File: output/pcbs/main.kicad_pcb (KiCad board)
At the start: 2 copper layers, 125.8 x 86.6 mm, 22 parts

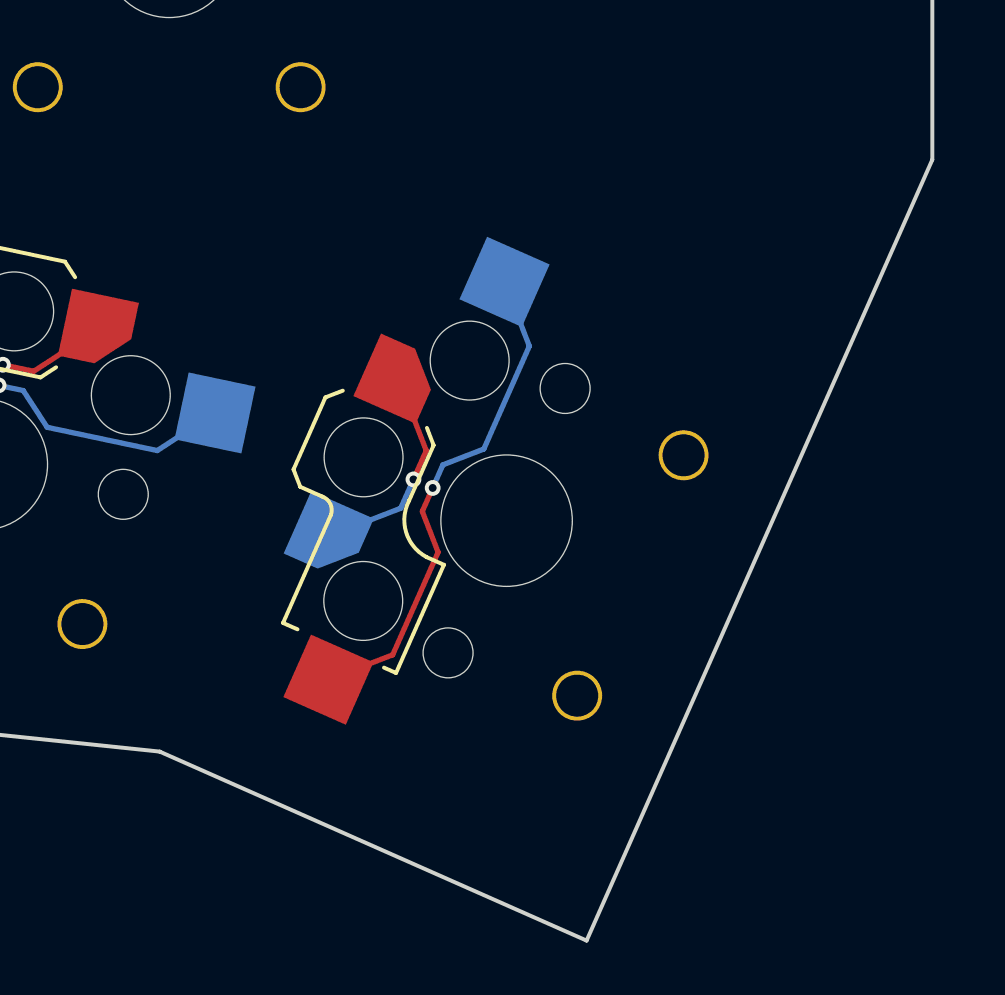
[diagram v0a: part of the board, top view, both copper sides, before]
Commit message: feat: add bottom ring bottom right corner ref
feat: add (bottom inner br, mcu tl) - (inner thumb tr, inner thumb tl)
lines intersection
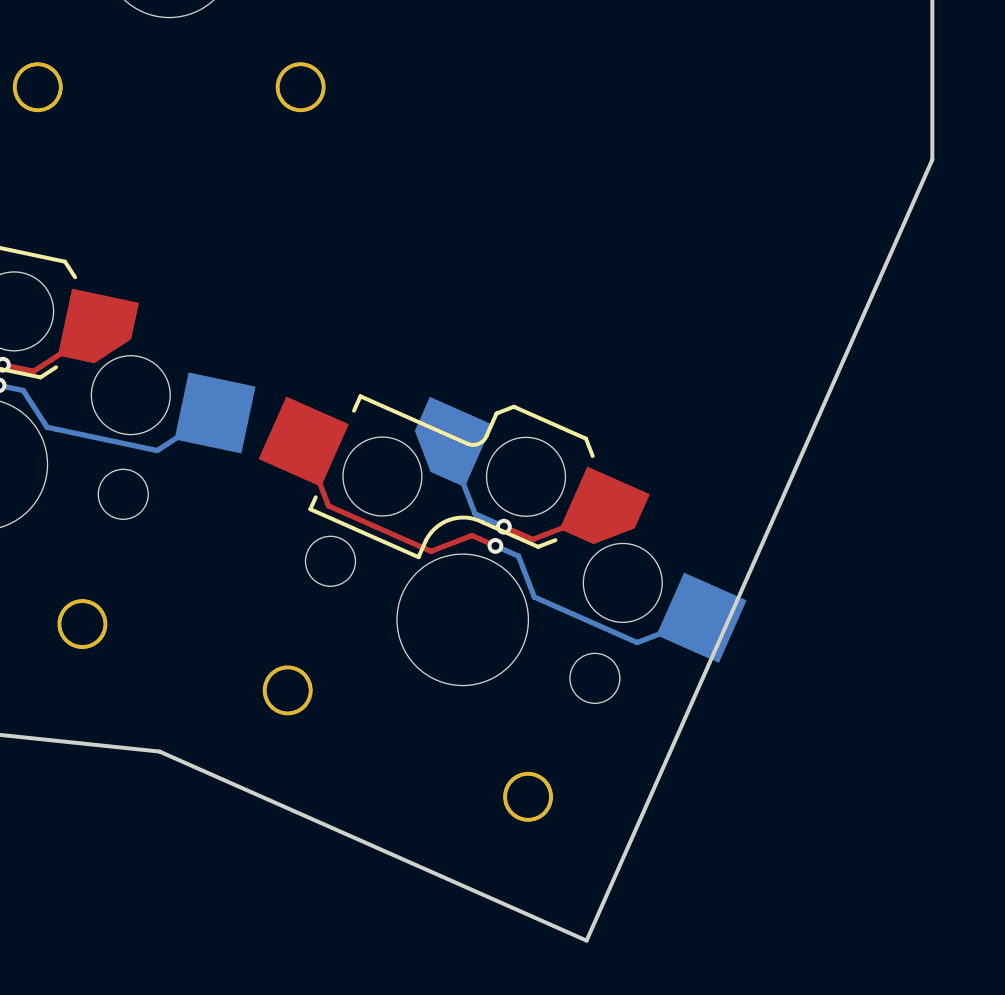
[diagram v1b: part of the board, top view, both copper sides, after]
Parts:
- moved S21 4.12 mm to (98.7, 23.0), turned to -23.88 degrees
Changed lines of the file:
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@@
   (footprint "ceoloide:switch_choc_v1_v2"
     (layer "B.Cu")
-    (at 100.3344316 19.2588836 66.12)
+    (at 98.6645391 23.0307643 -23.88)
     (property "Reference" "S21"
-      (at 0 8.8 66.12)
+      (at 0 8.8 -23.88)
       (layer "B.SilkS")
       hide
@@
     )
     (attr exclude_from_pos_files exclude_from_bom allow_soldermask_bridges)
-    (pad "" np_thru_hole circle (at 0 0 66.12) (size 5 5) (drill 5) (layers "*.Cu" "*.Mask"))
-    (pad "" np_thru_hole circle (at 5.5 0 66.12) (size 1.9 1.9) (drill 1.9) (layers "*.Cu" "*.Mask"))
-    (pad "" np_thru_hole circle (at -5.5 0 66.12) (size 1.9 1.9) (drill 1.9) (layers "*.Cu" "*.Mask"))
-    (pad "" thru_hole circle (at 5.00 5.15 66.12) (size 1.9 1.9) (drill 1.6) (layers "*.Cu" "*.Mask") )
-    (pad "" thru_hole circle (at -5.00 5.15 66.12) (size 1.9 1.9) (drill 1.6) (layers "*.Cu" "*.Mask") )
-    (pad "" np_thru_hole circle (at 0 -5.95 66.12) (size 3 3) (drill 3) (layers "*.Cu" "*.Mask"))
+    (pad "" np_thru_hole circle (at 0 0 -23.88) (size 5 5) (drill 5) (layers "*.Cu" "*.Mask"))
+    (pad "" np_thru_hole circle (at 5.5 0 -23.88) (size 1.9 1.9) (drill 1.9) (layers "*.Cu" "*.Mask"))
+    (pad "" np_thru_hole circle (at -5.5 0 -23.88) (size 1.9 1.9) (drill 1.9) (layers "*.Cu" "*.Mask"))
+    (pad "" thru_hole circle (at 5.00 5.15 -23.88) (size 1.9 1.9) (drill 1.6) (layers "*.Cu" "*.Mask") )
+    (pad "" thru_hole circle (at -5.00 5.15 -23.88) (size 1.9 1.9) (drill 1.6) (layers "*.Cu" "*.Mask") )
+    (pad "" np_thru_hole circle (at 0 -5.95 -23.88) (size 3 3) (drill 3) (layers "*.Cu" "*.Mask"))
     (fp_line (start -7 -5.6) (end -7 -6.2) (layer "F.SilkS") (stroke (width 0.15) (type solid)))
     (fp_line (start -7 -6.2) (end -2.52 -6.2) (layer "F.SilkS") (stroke (width 0.15) (type solid)))
@@
     (fp_line (start 2 -4.2) (end 1.5 -3.7) (layer "F.SilkS") (stroke (width 0.15) (type solid)))
     (fp_arc (start -2.5 -2.22) (mid -1.956518 -3.312082) (end -0.8 -3.7) (layer "F.SilkS") (stroke (width 0.15) (type solid)))
-    (pad "" np_thru_hole circle (at -5 -3.75 261.12) (size 3 3) (drill 3) (layers "*.Cu" "*.Mask"))
+    (pad "" np_thru_hole circle (at -5 -3.75 171.12) (size 3 3) (drill 3) (layers "*.Cu" "*.Mask"))
     (pad "1" smd roundrect
-      (at 3.275 -5.95 66.12)
+      (at 3.275 -5.95 -23.88)
       (size 2.6 2.6)
       (layers "F.Cu" "F.Paste" "F.Mask")
@@
       (net 0 "")
     )
-    (pad "2" smd rect (at -8.275 -3.75 66.12) (size 2.6 2.6) (layers "F.Cu" "F.Paste" "F.Mask") (net 24 "inner_cluster"))
+    (pad "2" smd rect (at -8.275 -3.75 -23.88) (size 2.6 2.6) (layers "F.Cu" "F.Paste" "F.Mask") (net 24 "inner_cluster"))
     (fp_line (start -1.5 -8.2) (end -2 -7.7) (layer "B.SilkS") (stroke (width 0.15) (type solid)))
     (fp_line (start 1.5 -8.2) (end -1.5 -8.2) (layer "B.SilkS") (stroke (width 0.15) (type solid)))
@@
     (fp_arc (start 0.8 -3.7) (mid 1.956518 -3.312082) (end 2.5 -2.22) (layer "B.SilkS") (stroke (width 0.15) (type solid)))
     (pad "1" smd roundrect
-      (at -3.275 -5.95 66.12)
+      (at -3.275 -5.95 -23.88)
       (size 2.6 2.6)
       (layers "B.Cu" "B.Paste" "B.Mask")
@@
       (net 0 "")
     )
-    (pad "2" smd rect (at 8.275 -3.75 66.12) (size 2.6 2.6) (layers "B.Cu" "B.Paste" "B.Mask") (net 24 "inner_cluster"))
-    (pad "" np_thru_hole circle (at 5 -3.75 261.12) (size 3 3) (drill 3) (layers "*.Cu" "*.Mask"))
+    (pad "2" smd rect (at 8.275 -3.75 -23.88) (size 2.6 2.6) (layers "B.Cu" "B.Paste" "B.Mask") (net 24 "inner_cluster"))
+    (pad "" np_thru_hole circle (at 5 -3.75 171.12) (size 3 3) (drill 3) (layers "*.Cu" "*.Mask"))
   )
 	(segment
-		(start 96.2195729 13.855545500000002)
-		(end 97.2769366 16.5929223)
+		(start 104.0678772 18.915905600000002)
+		(end 101.3305004 19.973269300000002)
 		(width 0.2)
 		(layer "F.Cu")
@@
 	)
 	(segment
-		(start 97.2769366 16.5929223)
-		(end 96.7911497 17.6901967)
+		(start 101.3305004 19.973269300000002)
+		(end 100.233226 19.4874824)
 		(width 0.2)
 		(layer "F.Cu")
@@
 	)
 	(via
-		(at 96.7911497 17.6901967)
+		(at 100.233226 19.4874824)
 		(size 0.6)
     (drill 0.3)
@@
 	)
 	(segment
-		(start 96.3053628 18.7874711)
-		(end 96.7911497 17.6901967)
+		(start 99.1359516 19.0016955)
+		(end 100.233226 19.4874824)
 		(width 0.2)
 		(layer "B.Cu")
@@
 	)
 	(segment
-		(start 93.567986 19.8448348)
-		(end 96.3053628 18.7874711)
+		(start 98.0785879 16.2643187)
+		(end 99.1359516 19.0016955)
 		(width 0.2)
 		(layer "B.Cu")
@@
 	)
 	(segment
-		(start 96.0013733 24.3626726)
-		(end 97.7287506 20.4609478)
+		(start 93.56075009999999 18.697706)
+		(end 97.4624749 20.4250833)
 		(width 0.2)
 		(layer "F.Cu")
@@
 	)
 	(segment
-		(start 97.1279641 18.9055901)
-		(end 97.522666 18.0140546)
+		(start 99.0178326 19.824296800000003)
+		(end 99.9093681 20.2189987)
 		(width 0.2)
 		(layer "F.Cu")
@@
 	)
 	(segment
-		(start 93.55554360000001 25.307420800000003)
-		(end 96.0013733 24.3626726)
+		(start 92.6160019 16.2518763)
+		(end 93.56075009999999 18.697706)
 		(width 0.2)
 		(layer "F.Cu")
@@
 	)
 	(segment
-		(start 97.7287506 20.4609478)
-		(end 97.1279641 18.9055901)
+		(start 97.4624749 20.4250833)
+		(end 99.0178326 19.824296800000003)
 		(width 0.2)
 		(layer "F.Cu")
@@
 	)
 	(via
-		(at 97.522666 18.0140546)
+		(at 99.9093681 20.2189987)
 		(size 0.6)
     (drill 0.3)
@@
 	)
 	(segment
-		(start 99.4671253 16.5343825)
-		(end 97.9117675 17.1351689)
+		(start 101.3890402 22.163458000000002)
+		(end 100.78825379999999 20.608100200000003)
 		(width 0.2)
 		(layer "B.Cu")
@@
 	)
 	(segment
-		(start 101.2001029 12.620007900000001)
-		(end 99.4671253 16.5343825)
+		(start 105.3034148 23.8964356)
+		(end 101.3890402 22.163458000000002)
 		(width 0.2)
 		(layer "B.Cu")
@@
 	)
 	(segment
-		(start 97.9117675 17.1351689)
-		(end 97.522666 18.0140546)
+		(start 100.78825379999999 20.608100200000003)
+		(end 99.9093681 20.2189987)
 		(width 0.2)
 		(layer "B.Cu")
@@
 	)
 	(segment
-		(start 100.2553547 10.1741782)
-		(end 101.2001029 12.620007900000001)
+		(start 107.7492445 22.9516874)
+		(end 105.3034148 23.8964356)
 		(width 0.2)
 		(layer "B.Cu")
@@
 (gr_line (start 96.75 -44.25) (end 96.75 -46.631) (layer Edge.Cuts) (stroke (width 0.15) (type default)))
 (gr_line (start 96.75 -46.631) (end 79.25 -46.631) (layer Edge.Cuts) (stroke (width 0.15) (type default)))
-(gr_line (start 103.3780884 35.2335285) (end 116.53 5.5265615) (layer Edge.Cuts) (stroke (width 0.15) (type default)))
+(gr_line (start 87.1375839 28.0435087) (end 103.3780884 35.233528500000006) (layer Edge.Cuts) (stroke (width 0.15) (type default)))
+(gr_line (start 103.3780884 35.233528500000006) (end 116.53 5.5265615) (layer Edge.Cuts) (stroke (width 0.15) (type default)))
 (gr_line (start 96.75 -44.25) (end 116.53 -44.25) (layer Edge.Cuts) (stroke (width 0.15) (type default)))
 (gr_line (start 116.53 -44.25) (end 116.53 5.5265615) (layer Edge.Cuts) (stroke (width 0.15) (type default)))
 (gr_line (start 43.75 9.25) (end 52 24.369) (layer Edge.Cuts) (stroke (width 0.15) (type default)))
 (gr_line (start 52 24.369) (end 87.1375839 28.0435087) (layer Edge.Cuts) (stroke (width 0.15) (type default)))
-(gr_line (start 87.1375839 28.0435087) (end 103.3780884 35.2335285) (layer Edge.Cuts) (stroke (width 0.15) (type default)))
 )

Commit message: feat: add ring bottom ref
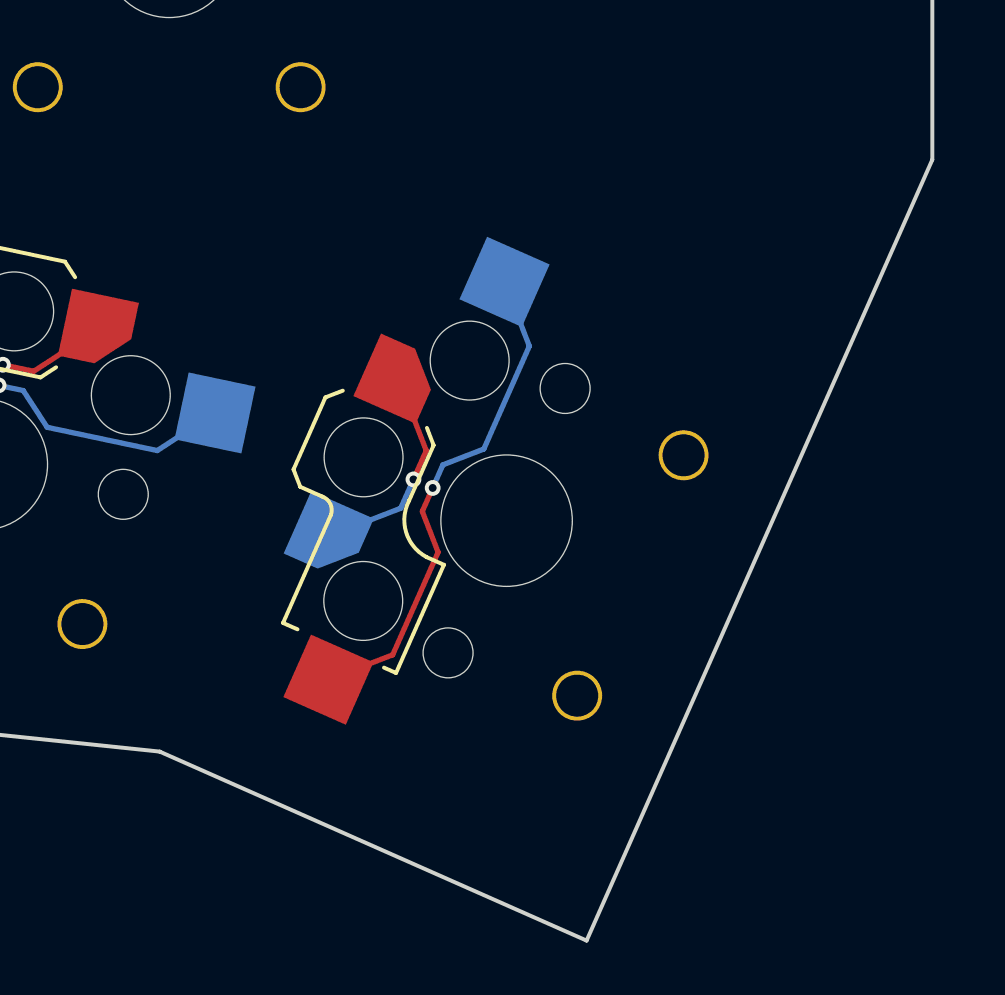
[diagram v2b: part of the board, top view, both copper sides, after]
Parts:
- moved S21 4.12 mm to (100.3, 19.3), turned to 66.12 degrees
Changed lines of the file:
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@@
   (footprint "ceoloide:switch_choc_v1_v2"
     (layer "B.Cu")
-    (at 98.6645391 23.0307643 -23.88)
+    (at 100.3344316 19.2588836 66.12)
     (property "Reference" "S21"
-      (at 0 8.8 -23.88)
+      (at 0 8.8 66.12)
       (layer "B.SilkS")
       hide
@@
     )
     (attr exclude_from_pos_files exclude_from_bom allow_soldermask_bridges)
-    (pad "" np_thru_hole circle (at 0 0 -23.88) (size 5 5) (drill 5) (layers "*.Cu" "*.Mask"))
-    (pad "" np_thru_hole circle (at 5.5 0 -23.88) (size 1.9 1.9) (drill 1.9) (layers "*.Cu" "*.Mask"))
-    (pad "" np_thru_hole circle (at -5.5 0 -23.88) (size 1.9 1.9) (drill 1.9) (layers "*.Cu" "*.Mask"))
-    (pad "" thru_hole circle (at 5.00 5.15 -23.88) (size 1.9 1.9) (drill 1.6) (layers "*.Cu" "*.Mask") )
-    (pad "" thru_hole circle (at -5.00 5.15 -23.88) (size 1.9 1.9) (drill 1.6) (layers "*.Cu" "*.Mask") )
-    (pad "" np_thru_hole circle (at 0 -5.95 -23.88) (size 3 3) (drill 3) (layers "*.Cu" "*.Mask"))
+    (pad "" np_thru_hole circle (at 0 0 66.12) (size 5 5) (drill 5) (layers "*.Cu" "*.Mask"))
+    (pad "" np_thru_hole circle (at 5.5 0 66.12) (size 1.9 1.9) (drill 1.9) (layers "*.Cu" "*.Mask"))
+    (pad "" np_thru_hole circle (at -5.5 0 66.12) (size 1.9 1.9) (drill 1.9) (layers "*.Cu" "*.Mask"))
+    (pad "" thru_hole circle (at 5.00 5.15 66.12) (size 1.9 1.9) (drill 1.6) (layers "*.Cu" "*.Mask") )
+    (pad "" thru_hole circle (at -5.00 5.15 66.12) (size 1.9 1.9) (drill 1.6) (layers "*.Cu" "*.Mask") )
+    (pad "" np_thru_hole circle (at 0 -5.95 66.12) (size 3 3) (drill 3) (layers "*.Cu" "*.Mask"))
     (fp_line (start -7 -5.6) (end -7 -6.2) (layer "F.SilkS") (stroke (width 0.15) (type solid)))
     (fp_line (start -7 -6.2) (end -2.52 -6.2) (layer "F.SilkS") (stroke (width 0.15) (type solid)))
@@
     (fp_line (start 2 -4.2) (end 1.5 -3.7) (layer "F.SilkS") (stroke (width 0.15) (type solid)))
     (fp_arc (start -2.5 -2.22) (mid -1.956518 -3.312082) (end -0.8 -3.7) (layer "F.SilkS") (stroke (width 0.15) (type solid)))
-    (pad "" np_thru_hole circle (at -5 -3.75 171.12) (size 3 3) (drill 3) (layers "*.Cu" "*.Mask"))
+    (pad "" np_thru_hole circle (at -5 -3.75 261.12) (size 3 3) (drill 3) (layers "*.Cu" "*.Mask"))
     (pad "1" smd roundrect
-      (at 3.275 -5.95 -23.88)
+      (at 3.275 -5.95 66.12)
       (size 2.6 2.6)
       (layers "F.Cu" "F.Paste" "F.Mask")
@@
       (net 0 "")
     )
-    (pad "2" smd rect (at -8.275 -3.75 -23.88) (size 2.6 2.6) (layers "F.Cu" "F.Paste" "F.Mask") (net 24 "inner_cluster"))
+    (pad "2" smd rect (at -8.275 -3.75 66.12) (size 2.6 2.6) (layers "F.Cu" "F.Paste" "F.Mask") (net 24 "inner_cluster"))
     (fp_line (start -1.5 -8.2) (end -2 -7.7) (layer "B.SilkS") (stroke (width 0.15) (type solid)))
     (fp_line (start 1.5 -8.2) (end -1.5 -8.2) (layer "B.SilkS") (stroke (width 0.15) (type solid)))
@@
     (fp_arc (start 0.8 -3.7) (mid 1.956518 -3.312082) (end 2.5 -2.22) (layer "B.SilkS") (stroke (width 0.15) (type solid)))
     (pad "1" smd roundrect
-      (at -3.275 -5.95 -23.88)
+      (at -3.275 -5.95 66.12)
       (size 2.6 2.6)
       (layers "B.Cu" "B.Paste" "B.Mask")
@@
       (net 0 "")
     )
-    (pad "2" smd rect (at 8.275 -3.75 -23.88) (size 2.6 2.6) (layers "B.Cu" "B.Paste" "B.Mask") (net 24 "inner_cluster"))
-    (pad "" np_thru_hole circle (at 5 -3.75 171.12) (size 3 3) (drill 3) (layers "*.Cu" "*.Mask"))
+    (pad "2" smd rect (at 8.275 -3.75 66.12) (size 2.6 2.6) (layers "B.Cu" "B.Paste" "B.Mask") (net 24 "inner_cluster"))
+    (pad "" np_thru_hole circle (at 5 -3.75 261.12) (size 3 3) (drill 3) (layers "*.Cu" "*.Mask"))
   )
 	(segment
-		(start 104.0678772 18.915905600000002)
-		(end 101.3305004 19.973269300000002)
+		(start 96.2195729 13.855545500000002)
+		(end 97.2769366 16.5929223)
 		(width 0.2)
 		(layer "F.Cu")
@@
 	)
 	(segment
-		(start 101.3305004 19.973269300000002)
-		(end 100.233226 19.4874824)
+		(start 97.2769366 16.5929223)
+		(end 96.7911497 17.6901967)
 		(width 0.2)
 		(layer "F.Cu")
@@
 	)
 	(via
-		(at 100.233226 19.4874824)
+		(at 96.7911497 17.6901967)
 		(size 0.6)
     (drill 0.3)
@@
 	)
 	(segment
-		(start 99.1359516 19.0016955)
-		(end 100.233226 19.4874824)
+		(start 96.3053628 18.7874711)
+		(end 96.7911497 17.6901967)
 		(width 0.2)
 		(layer "B.Cu")
@@
 	)
 	(segment
-		(start 98.0785879 16.2643187)
-		(end 99.1359516 19.0016955)
+		(start 93.567986 19.8448348)
+		(end 96.3053628 18.7874711)
 		(width 0.2)
 		(layer "B.Cu")
@@
 	)
 	(segment
-		(start 93.56075009999999 18.697706)
-		(end 97.4624749 20.4250833)
+		(start 96.0013733 24.3626726)
+		(end 97.7287506 20.4609478)
 		(width 0.2)
 		(layer "F.Cu")
@@
 	)
 	(segment
-		(start 99.0178326 19.824296800000003)
-		(end 99.9093681 20.2189987)
+		(start 97.1279641 18.9055901)
+		(end 97.522666 18.0140546)
 		(width 0.2)
 		(layer "F.Cu")
@@
 	)
 	(segment
-		(start 92.6160019 16.2518763)
-		(end 93.56075009999999 18.697706)
+		(start 93.55554360000001 25.307420800000003)
+		(end 96.0013733 24.3626726)
 		(width 0.2)
 		(layer "F.Cu")
@@
 	)
 	(segment
-		(start 97.4624749 20.4250833)
-		(end 99.0178326 19.824296800000003)
+		(start 97.7287506 20.4609478)
+		(end 97.1279641 18.9055901)
 		(width 0.2)
 		(layer "F.Cu")
@@
 	)
 	(via
-		(at 99.9093681 20.2189987)
+		(at 97.522666 18.0140546)
 		(size 0.6)
     (drill 0.3)
@@
 	)
 	(segment
-		(start 101.3890402 22.163458000000002)
-		(end 100.78825379999999 20.608100200000003)
+		(start 99.4671253 16.5343825)
+		(end 97.9117675 17.1351689)
 		(width 0.2)
 		(layer "B.Cu")
@@
 	)
 	(segment
-		(start 105.3034148 23.8964356)
-		(end 101.3890402 22.163458000000002)
+		(start 101.2001029 12.620007900000001)
+		(end 99.4671253 16.5343825)
 		(width 0.2)
 		(layer "B.Cu")
@@
 	)
 	(segment
-		(start 100.78825379999999 20.608100200000003)
-		(end 99.9093681 20.2189987)
+		(start 97.9117675 17.1351689)
+		(end 97.522666 18.0140546)
 		(width 0.2)
 		(layer "B.Cu")
@@
 	)
 	(segment
-		(start 107.7492445 22.9516874)
-		(end 105.3034148 23.8964356)
+		(start 100.2553547 10.1741782)
+		(end 101.2001029 12.620007900000001)
 		(width 0.2)
 		(layer "B.Cu")
@@
 (gr_line (start 96.75 -44.25) (end 96.75 -46.631) (layer Edge.Cuts) (stroke (width 0.15) (type default)))
 (gr_line (start 96.75 -46.631) (end 79.25 -46.631) (layer Edge.Cuts) (stroke (width 0.15) (type default)))
-(gr_line (start 87.1375839 28.0435087) (end 103.3780884 35.233528500000006) (layer Edge.Cuts) (stroke (width 0.15) (type default)))
-(gr_line (start 103.3780884 35.233528500000006) (end 116.53 5.5265615) (layer Edge.Cuts) (stroke (width 0.15) (type default)))
+(gr_line (start 103.3780884 35.2335285) (end 116.53 5.5265615) (layer Edge.Cuts) (stroke (width 0.15) (type default)))
 (gr_line (start 96.75 -44.25) (end 116.53 -44.25) (layer Edge.Cuts) (stroke (width 0.15) (type default)))
 (gr_line (start 116.53 -44.25) (end 116.53 5.5265615) (layer Edge.Cuts) (stroke (width 0.15) (type default)))
 (gr_line (start 43.75 9.25) (end 52 24.369) (layer Edge.Cuts) (stroke (width 0.15) (type default)))
 (gr_line (start 52 24.369) (end 87.1375839 28.0435087) (layer Edge.Cuts) (stroke (width 0.15) (type default)))
+(gr_line (start 87.1375839 28.0435087) (end 103.3780884 35.2335285) (layer Edge.Cuts) (stroke (width 0.15) (type default)))
 )
